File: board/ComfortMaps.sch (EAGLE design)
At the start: 42 parts, among them J1 PROG_HDR, J5 0545482271, J6 0545482271, U1 ADXL362, U3 ADP160-3.3, U4 MCP73833, X1 RASPI_GPIO_B+#_PIN

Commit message: Updating board, needs components on digikey.
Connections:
- net GND: now also X1.GND_A, X1.GND_B, X1.GND_C, X1.GND_D, X1.GND_E, X1.GND_F, X1.GND_G, X1.GND_H
- net VOUT: now also X1.5V0A, X1.5V0B; no longer X1.3V3A
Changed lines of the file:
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@@
 <part name="J5" library="0545482271" deviceset="0545482271" device=""/>
 <part name="J6" library="0545482271" deviceset="0545482271" device=""/>
+<part name="GND8" library="SparkFun-Aesthetics" deviceset="GND" device=""/>
 </parts>
 <sheets>
@@
 <attribute name="NAME" x="326.39" y="147.32" size="1.778" layer="95" align="center-left"/>
 <attribute name="VALUE" x="326.39" y="144.78" size="1.778" layer="96" align="center-left"/>
+</instance>
+<instance part="GND8" gate="1" x="330.2" y="20.32" smashed="yes">
+<attribute name="VALUE" x="327.66" y="17.78" size="1.778" layer="96"/>
 </instance>
 </instances>
@@
 </segment>
 <segment>
-<pinref part="X1" gate="G$1" pin="3V3A"/>
-<wire x1="309.88" y1="93.98" x2="309.88" y2="104.14" width="0.1524" layer="91"/>
-<label x="309.88" y="104.14" size="1.778" layer="95" xref="yes"/>
+<label x="297.18" y="104.14" size="1.778" layer="95" xref="yes"/>
+<pinref part="X1" gate="G$1" pin="5V0A"/>
+<wire x1="297.18" y1="93.98" x2="297.18" y2="99.06" width="0.1524" layer="91"/>
+<pinref part="X1" gate="G$1" pin="5V0B"/>
+<wire x1="297.18" y1="99.06" x2="297.18" y2="104.14" width="0.1524" layer="91"/>
+<wire x1="299.72" y1="93.98" x2="299.72" y2="99.06" width="0.1524" layer="91"/>
+<wire x1="299.72" y1="99.06" x2="297.18" y2="99.06" width="0.1524" layer="91"/>
+<junction x="297.18" y="99.06"/>
 </segment>
 </net>
@@
 <pinref part="GND19" gate="1" pin="GND"/>
 </segment>
+<segment>
+<pinref part="X1" gate="G$1" pin="GND_A"/>
+<pinref part="GND8" gate="1" pin="GND"/>
+<wire x1="320.04" y1="58.42" x2="330.2" y2="58.42" width="0.1524" layer="91"/>
+<wire x1="330.2" y1="58.42" x2="330.2" y2="55.88" width="0.1524" layer="91"/>
+<pinref part="X1" gate="G$1" pin="GND_B"/>
+<wire x1="330.2" y1="55.88" x2="330.2" y2="53.34" width="0.1524" layer="91"/>
+<wire x1="330.2" y1="53.34" x2="330.2" y2="50.8" width="0.1524" layer="91"/>
+<wire x1="330.2" y1="50.8" x2="330.2" y2="48.26" width="0.1524" layer="91"/>
+<wire x1="330.2" y1="48.26" x2="330.2" y2="45.72" width="0.1524" layer="91"/>
+<wire x1="330.2" y1="45.72" x2="330.2" y2="43.18" width="0.1524" layer="91"/>
+<wire x1="330.2" y1="43.18" x2="330.2" y2="40.64" width="0.1524" layer="91"/>
+<wire x1="330.2" y1="40.64" x2="330.2" y2="22.86" width="0.1524" layer="91"/>
+<wire x1="320.04" y1="55.88" x2="330.2" y2="55.88" width="0.1524" layer="91"/>
+<junction x="330.2" y="55.88"/>
+<pinref part="X1" gate="G$1" pin="GND_C"/>
+<wire x1="320.04" y1="53.34" x2="330.2" y2="53.34" width="0.1524" layer="91"/>
+<junction x="330.2" y="53.34"/>
+<pinref part="X1" gate="G$1" pin="GND_D"/>
+<wire x1="320.04" y1="50.8" x2="330.2" y2="50.8" width="0.1524" layer="91"/>
+<junction x="330.2" y="50.8"/>
+<pinref part="X1" gate="G$1" pin="GND_E"/>
+<wire x1="320.04" y1="48.26" x2="330.2" y2="48.26" width="0.1524" layer="91"/>
+<junction x="330.2" y="48.26"/>
+<pinref part="X1" gate="G$1" pin="GND_F"/>
+<wire x1="320.04" y1="45.72" x2="330.2" y2="45.72" width="0.1524" layer="91"/>
+<junction x="330.2" y="45.72"/>
+<pinref part="X1" gate="G$1" pin="GND_G"/>
+<wire x1="320.04" y1="43.18" x2="330.2" y2="43.18" width="0.1524" layer="91"/>
+<junction x="330.2" y="43.18"/>
+<pinref part="X1" gate="G$1" pin="GND_H"/>
+<wire x1="320.04" y1="40.64" x2="330.2" y2="40.64" width="0.1524" layer="91"/>
+<junction x="330.2" y="40.64"/>
+</segment>
 </net>

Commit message: Soldering first board.
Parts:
- added R13, R14, R15, R16, R9: 10k, SparkFun-Resistors:10K-1%RES-00824
- S1, S2, S3, S4, S5: value MOMENTARY-SWITCH-SPST-SMD-12MM -> SPST-12MM
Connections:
- net VDD renamed V_USB
- net 3.3V: now also R13.2, R14.2, R15.2, R16.2, R9.2; no longer S1.1, S2.1, S3.1, S4.1, S5.1
- net GND: now also S1.1, S2.1, S3.1, S4.1, S5.1
- net GPIO17: now also R9.1
- net GPIO18: now also R13.1
- net GPIO22: now also R15.1
- net GPIO23: now also R16.1
- net GPIO27: now also R14.1
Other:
- note added: "VBUS: 3.75 - 6V"
- note removed: "VDD: 3.75 - 6V"
- moved on the sheet: S2, S3, S4, S5

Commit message: Latest, before upwork.
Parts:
- removed JP1: FTDI_DEVICE, SparkFun-Connectors:FTDI_DEVICE
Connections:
- new net TX0: X1.RXD
- net GND: no longer JP1.GND
- net RXI: now also X1.TXD; no longer JP1.RXI
- net TXO: no longer JP1.TXO
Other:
- note added: "Rev 2"
- note removed: "Rev 1"
- moved on the sheet: R4
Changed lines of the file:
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@@
 <?xml version="1.0" encoding="utf-8"?>
 <!DOCTYPE eagle SYSTEM "eagle.dtd">
-<eagle version="9.5.1">
+<eagle version="9.5.2">
 <drawing>
 <settings>
@@
 </part>
 <part name="JP3" library="SparkFun-Connectors" deviceset="M03" device="PTH"/>
-<part name="JP1" library="SparkFun-Connectors" deviceset="FTDI_DEVICE" device=""/>
 <part name="D2" library="SparkFun-DiscreteSemi" deviceset="DIODE-SCHOTTKY" device="" value="RB751">
 <attribute name="PROD_ID" value="DIO-11018"/>
@@
 </part>
 <part name="P+6" library="SparkFun-Aesthetics" deviceset="3.3V" device=""/>
-<part name="GND7" library="SparkFun-Aesthetics" deviceset="GND" device=""/>
 <part name="R4" library="SparkFun-Resistors" deviceset="10K-1%" device="RES-00824" value="10k">
 <attribute name="PROD_ID" value="RES-00824"/>
@@
 <sheet>
 <plain>
-<text x="238.252" y="5.842" size="5.08" layer="94">Rev 1</text>
+<text x="238.252" y="5.842" size="5.08" layer="94">Rev 2</text>
 <text x="2.54" y="2.54" size="1.778" layer="94">Original wake-on-shake concept by
 Nitzan Gadish, Analog Devices</text>
@@
 <attribute name="NAME" x="119.38" y="62.738" size="1.778" layer="95" rot="R180"/>
 </instance>
-<instance part="JP1" gate="G$1" x="162.56" y="33.02" smashed="yes">
-<attribute name="NAME" x="162.56" y="43.18" size="1.778" layer="95"/>
-<attribute name="VALUE" x="162.56" y="40.64" size="1.778" layer="96"/>
-</instance>
 <instance part="D2" gate="G$1" x="66.04" y="45.72" smashed="yes">
 <attribute name="PROD_ID" x="66.04" y="45.72" size="1.778" layer="96" display="off"/>
@@
 <attribute name="VALUE" x="16.764" y="140.716" size="1.778" layer="96"/>
 </instance>
-<instance part="GND7" gate="1" x="152.4" y="20.32" smashed="yes">
-<attribute name="VALUE" x="149.86" y="17.78" size="1.778" layer="96"/>
-</instance>
-<instance part="R4" gate="G$1" x="147.32" y="40.64" smashed="yes">
-<attribute name="PROD_ID" x="147.32" y="40.64" size="1.778" layer="96" display="off"/>
-<attribute name="NAME" x="143.51" y="42.1386" size="1.778" layer="95"/>
-<attribute name="VALUE" x="143.51" y="37.338" size="1.778" layer="96"/>
-</instance>
-<instance part="P+7" gate="G$1" x="139.7" y="43.18" smashed="yes">
-<attribute name="VALUE" x="138.684" y="46.736" size="1.778" layer="96"/>
+<instance part="R4" gate="G$1" x="327.66" y="73.66" smashed="yes" rot="R270">
+<attribute name="PROD_ID" x="327.66" y="73.66" size="1.778" layer="96" rot="R270" display="off"/>
+<attribute name="NAME" x="329.1586" y="77.47" size="1.778" layer="95" rot="R270"/>
+<attribute name="VALUE" x="324.358" y="77.47" size="1.778" layer="96" rot="R270"/>
+</instance>
+<instance part="P+7" gate="G$1" x="327.66" y="101.6" smashed="yes">
+<attribute name="VALUE" x="326.644" y="105.156" size="1.778" layer="96"/>
 </instance>
 <instance part="S1" gate="G$1" x="218.44" y="81.28" smashed="yes">
@@
 <pinref part="GND6" gate="1" pin="GND"/>
 <wire x1="167.64" y1="66.04" x2="167.64" y2="63.5" width="0.1524" layer="91"/>
-</segment>
-<segment>
-<pinref part="JP1" gate="G$1" pin="GND"/>
-<wire x1="157.48" y1="25.4" x2="152.4" y2="25.4" width="0.1524" layer="91"/>
-<wire x1="152.4" y1="25.4" x2="152.4" y2="22.86" width="0.1524" layer="91"/>
-<pinref part="GND7" gate="1" pin="GND"/>
 </segment>
 <segment>
@@
 <segment>
 <pinref part="P+7" gate="G$1" pin="3.3V"/>
-<wire x1="139.7" y1="43.18" x2="139.7" y2="40.64" width="0.1524" layer="91"/>
+<wire x1="327.66" y1="101.6" x2="327.66" y2="78.74" width="0.1524" layer="91"/>
 <pinref part="R4" gate="G$1" pin="1"/>
-<wire x1="139.7" y1="40.64" x2="142.24" y2="40.64" width="0.1524" layer="91"/>
 </segment>
 <segment>
@@
 </segment>
 <segment>
-<pinref part="JP1" gate="G$1" pin="RXI"/>
-<wire x1="157.48" y1="33.02" x2="154.94" y2="33.02" width="0.1524" layer="91"/>
-<label x="142.24" y="33.02" size="1.27" layer="95" rot="R180" xref="yes"/>
+<pinref part="X1" gate="G$1" pin="TXD"/>
+<wire x1="320.04" y1="66.04" x2="327.66" y2="66.04" width="0.1524" layer="91"/>
+<label x="330.2" y="66.04" size="1.778" layer="95" xref="yes"/>
 <pinref part="R4" gate="G$1" pin="2"/>
-<wire x1="154.94" y1="33.02" x2="142.24" y2="33.02" width="0.1524" layer="91"/>
-<wire x1="152.4" y1="40.64" x2="154.94" y2="40.64" width="0.1524" layer="91"/>
-<wire x1="154.94" y1="40.64" x2="154.94" y2="33.02" width="0.1524" layer="91"/>
-<junction x="154.94" y="33.02"/>
+<wire x1="327.66" y1="66.04" x2="330.2" y2="66.04" width="0.1524" layer="91"/>
+<wire x1="327.66" y1="68.58" x2="327.66" y2="66.04" width="0.1524" layer="91"/>
+<junction x="327.66" y="66.04"/>
 </segment>
 </net>
@@
 <wire x1="33.02" y1="129.54" x2="25.4" y2="129.54" width="0.1524" layer="91"/>
 <label x="25.4" y="129.54" size="1.27" layer="95" rot="R180" xref="yes"/>
-</segment>
-<segment>
-<pinref part="JP1" gate="G$1" pin="TXO"/>
-<wire x1="157.48" y1="35.56" x2="142.24" y2="35.56" width="0.1524" layer="91"/>
-<label x="142.24" y="35.56" size="1.27" layer="95" rot="R180" xref="yes"/>
 </segment>
 </net>
@@
 </segment>
 </net>
+<net name="TX0" class="0">
+<segment>
+<pinref part="X1" gate="G$1" pin="RXD"/>
+<wire x1="320.04" y1="63.5" x2="330.2" y2="63.5" width="0.1524" layer="91"/>
+<label x="330.2" y="63.5" size="1.778" layer="95" xref="yes"/>
+</segment>
+</net>

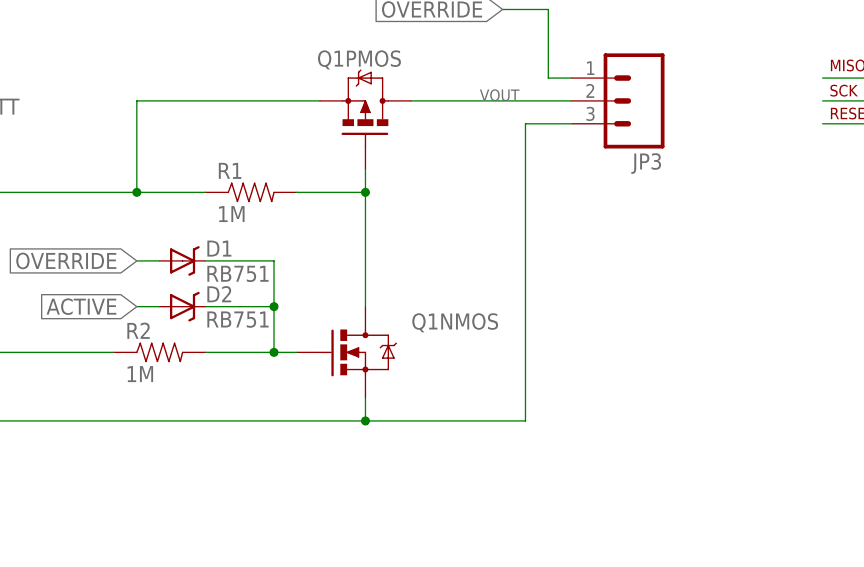
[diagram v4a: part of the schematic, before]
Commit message: Switching to larger schottke diode.
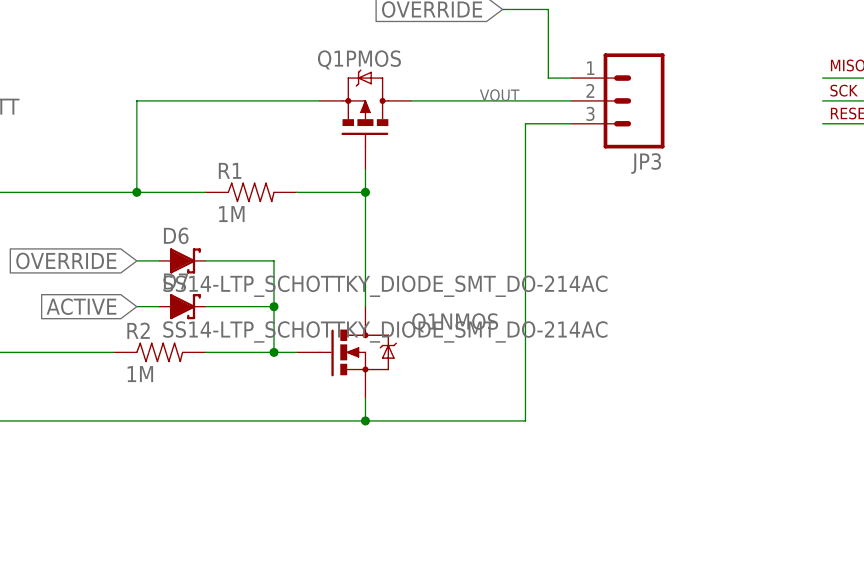
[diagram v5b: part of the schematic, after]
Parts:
- removed D1: RB751, SparkFun-DiscreteSemi:RB751
- removed D2: RB751, SparkFun-DiscreteSemi:DIODE-SCHOTTKY
- added D6, D7: SS14-LTP_SCHOTTKY_DIODE_SMT_DO-214AC, DIODE SCHOTTKY 1A 40V SMA:SS14-LTP_SCHOTTKY_DIODE_SMT_DO-214AC
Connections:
- net ACTIVE: now also D7.A; no longer D2.A
- net N$2: now also D6.C, D7.C; no longer D1.C, D2.C
- net OVERRIDE: now also D6.A; no longer D1.A
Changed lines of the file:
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@@
 <?xml version="1.0" encoding="utf-8"?>
 <!DOCTYPE eagle SYSTEM "eagle.dtd">
-<eagle version="9.5.2">
+<eagle version="9.5.1">
 <drawing>
 <settings>
@@
 <layer number="59" name="tCarbon" color="7" fill="1" visible="no" active="no"/>
 <layer number="60" name="bCarbon" color="7" fill="1" visible="no" active="no"/>
+<layer number="61" name="stand" color="7" fill="1" visible="no" active="no"/>
 <layer number="88" name="SimResults" color="9" fill="1" visible="yes" active="yes"/>
 <layer number="89" name="SimProbes" color="9" fill="1" visible="yes" active="yes"/>
@@
 <layer number="115" name="ReferenceISLANDS" color="7" fill="1" visible="yes" active="yes"/>
 <layer number="116" name="Patch_BOT" color="9" fill="4" visible="no" active="yes"/>
+<layer number="117" name="BACKMAAT1" color="7" fill="1" visible="yes" active="yes"/>
 <layer number="118" name="Rect_Pads" color="7" fill="1" visible="no" active="yes"/>
+<layer number="119" name="KAP_TEKEN" color="7" fill="1" visible="yes" active="yes"/>
+<layer number="120" name="KAP_MAAT1" color="7" fill="1" visible="yes" active="yes"/>
 <layer number="121" name="_tsilk" color="7" fill="1" visible="no" active="yes"/>
 <layer number="122" name="_bsilk" color="7" fill="1" visible="no" active="yes"/>
@@
 <layer number="128" name="_bValues" color="7" fill="1" visible="no" active="yes"/>
 <layer number="129" name="Mask" color="7" fill="1" visible="no" active="yes"/>
+<layer number="130" name="SMDSTROOK" color="7" fill="1" visible="yes" active="yes"/>
 <layer number="131" name="tAdjust" color="7" fill="1" visible="no" active="yes"/>
 <layer number="132" name="bAdjust" color="7" fill="1" visible="no" active="yes"/>
+<layer number="133" name="bottom_silk" color="7" fill="1" visible="yes" active="yes"/>
+<layer number="134" name="silk_top" color="7" fill="1" visible="yes" active="yes"/>
+<layer number="135" name="silk_bottom" color="7" fill="1" visible="yes" active="yes"/>
+<layer number="136" name="silktop" color="7" fill="1" visible="yes" active="yes"/>
+<layer number="137" name="silkbottom" color="7" fill="1" visible="yes" active="yes"/>
+<layer number="138" name="SLOTS" color="7" fill="1" visible="yes" active="yes"/>
 <layer number="144" name="Drill_legend" color="7" fill="1" visible="no" active="yes"/>
+<layer number="145" name="DrillLegend_01-16" color="7" fill="1" visible="yes" active="yes"/>
+<layer number="146" name="DrillLegend_01-20" color="7" fill="1" visible="yes" active="yes"/>
 <layer number="150" name="Notes" color="7" fill="1" visible="no" active="yes"/>
 <layer number="151" name="HeatSink" color="7" fill="1" visible="no" active="yes"/>
@@
 <layer number="232" name="Eagle3D_PG2" color="7" fill="1" visible="yes" active="yes"/>
 <layer number="233" name="Eagle3D_PG3" color="7" fill="1" visible="yes" active="yes"/>
+<layer number="234" name="Input" color="7" fill="1" visible="yes" active="yes"/>
 <layer number="248" name="Housing" color="7" fill="1" visible="no" active="yes"/>
 <layer number="249" name="Edge" color="7" fill="1" visible="no" active="yes"/>
@@
 <attribute name="PROD_ID" value="CAP-00810"/>
 </part>
-<part name="D1" library="SparkFun-DiscreteSemi" deviceset="RB751" device="" value="RB751">
-<attribute name="PROD_ID" value="DIO-11018"/>
-</part>
 <part name="JP3" library="SparkFun-Connectors" deviceset="M03" device="PTH"/>
-<part name="D2" library="SparkFun-DiscreteSemi" deviceset="DIODE-SCHOTTKY" device="" value="RB751">
-<attribute name="PROD_ID" value="DIO-11018"/>
-</part>
 <part name="U3" library="SparkFun-PowerIC" deviceset="ADP160" device="" value="ADP160-3.3">
 <attribute name="DIST" value="Digikey"/>
@@
 <part name="R16" library="SparkFun-Resistors" deviceset="10K-1%" device="RES-00824" value="10k"/>
 <part name="GND20" library="SparkFun-Aesthetics" deviceset="GND" device=""/>
+<part name="D6" library="DIODE SCHOTTKY 1A 40V SMA" deviceset="SS14-LTP_SCHOTTKY_DIODE_SMT_DO-214AC" device=""/>
+<part name="D7" library="DIODE SCHOTTKY 1A 40V SMA" deviceset="SS14-LTP_SCHOTTKY_DIODE_SMT_DO-214AC" device=""/>
 </parts>
 <sheets>
@@
 <attribute name="VALUE" x="176.784" y="122.301" size="1.778" layer="96"/>
 </instance>
-<instance part="D1" gate="G$1" x="66.04" y="50.8" smashed="yes">
-<attribute name="PROD_ID" x="66.04" y="50.8" size="1.778" layer="96" display="off"/>
-<attribute name="NAME" x="68.58" y="51.2826" size="1.778" layer="95"/>
-<attribute name="VALUE" x="68.58" y="48.4886" size="1.778" layer="96"/>
-</instance>
 <instance part="JP3" gate="G$1" x="116.84" y="68.58" smashed="yes" rot="R180">
 <attribute name="VALUE" x="119.38" y="76.2" size="1.778" layer="96" rot="R180"/>
 <attribute name="NAME" x="119.38" y="62.738" size="1.778" layer="95" rot="R180"/>
-</instance>
-<instance part="D2" gate="G$1" x="66.04" y="45.72" smashed="yes">
-<attribute name="PROD_ID" x="66.04" y="45.72" size="1.778" layer="96" display="off"/>
-<attribute name="NAME" x="68.58" y="46.2026" size="1.778" layer="95"/>
-<attribute name="VALUE" x="68.58" y="43.4086" size="1.778" layer="96"/>
 </instance>
 <instance part="U3" gate="G$1" x="289.56" y="177.8" smashed="yes">
@@
 <instance part="GND20" gate="1" x="198.12" y="10.16" smashed="yes">
 <attribute name="VALUE" x="195.58" y="7.62" size="1.778" layer="96"/>
+</instance>
+<instance part="D6" gate="1" x="66.04" y="50.8" smashed="yes">
+<attribute name="NAME" x="63.754" y="52.705" size="1.778" layer="95"/>
+<attribute name="VALUE" x="63.754" y="47.371" size="1.778" layer="96"/>
+</instance>
+<instance part="D7" gate="1" x="66.04" y="45.72" smashed="yes">
+<attribute name="NAME" x="63.754" y="47.625" size="1.778" layer="95"/>
+<attribute name="VALUE" x="63.754" y="42.291" size="1.778" layer="96"/>
 </instance>
 </instances>
@@
 <net name="N$2" class="0">
 <segment>
-<pinref part="D1" gate="G$1" pin="C"/>
 <wire x1="68.58" y1="50.8" x2="76.2" y2="50.8" width="0.1524" layer="91"/>
 <pinref part="Q1" gate="NMOS" pin="G"/>
@@
 <wire x1="76.2" y1="50.8" x2="76.2" y2="45.72" width="0.1524" layer="91"/>
 <junction x="76.2" y="40.64"/>
-<pinref part="D2" gate="G$1" pin="C"/>
 <wire x1="76.2" y1="45.72" x2="76.2" y2="40.64" width="0.1524" layer="91"/>
 <wire x1="68.58" y1="45.72" x2="76.2" y2="45.72" width="0.1524" layer="91"/>
 <junction x="76.2" y="45.72"/>
+<pinref part="D6" gate="1" pin="C"/>
+<pinref part="D7" gate="1" pin="C"/>
 </segment>
 </net>
@@
 <net name="OVERRIDE" class="0">
 <segment>
-<pinref part="D1" gate="G$1" pin="A"/>
 <wire x1="63.5" y1="50.8" x2="60.96" y2="50.8" width="0.1524" layer="91"/>
 <label x="60.96" y="50.8" size="1.778" layer="95" rot="R180" xref="yes"/>
+<pinref part="D6" gate="1" pin="A"/>
 </segment>
 <segment>
@@
 <net name="ACTIVE" class="0">
 <segment>
-<pinref part="D2" gate="G$1" pin="A"/>
 <wire x1="63.5" y1="45.72" x2="60.96" y2="45.72" width="0.1524" layer="91"/>
 <label x="60.96" y="45.72" size="1.778" layer="95" rot="R180" xref="yes"/>
-</segment>
-<segment>
+<pinref part="D7" gate="1" pin="A"/>
+</segment>
+<segment>
